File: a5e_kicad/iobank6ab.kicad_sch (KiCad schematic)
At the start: 1 part, among them U7 A5EB013B-B23B

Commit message: Power/config review against the Altera docs: bank 6A, MSEL, resets, fabric clock
Checked against Pin Connection Guidelines 813266, Power Management UG
813161, Configuration UG 813773 and the data sheet 813918; findings are
in AGILEX_POWER_CONFIG_CHECKLIST.md.

- VCCIO_HVIO_6A moves from the VCCPT 1V8 regulator to 3V3. PCG table 32
  requires a dedicated VCCIO_HVIO supply. CE19 no longer takes the 1.8 V
  sdm_clk25.
- Y4 (YXC OT3225100MJBA4SL, 100 MHz 3.3 V CMOS, C4353707) drives the
  dangling clk100 net to AE11 (bank 6G PLLREFCLK1), giving the fabric a
  PLL reference that doesn't depend on the HPS. The clock sheet pin
  clk2_N is renamed clk100.
- MSEL 001 (AS fast) -> 011 (AS normal): fast mode needs all supplies
  ramped within 10 ms, which the sequenced regulators don't guarantee.
  R45 now goes to 1V8, and R4 gets its own GND.
- R264 10k pull-up on HPS_COLD_nRESET (SDM_IO10), as the PCG requires.
- R9/R10 (INIT_DONE/CONF_DONE pull-ups) DNP; the internal pull-downs
  hold the pins low until configuration.
- Note on the fpga_power sheet and the PCB (Cmts.User): ferrite + cap
  isolation filters on the PLL/ADC rails are recommended but not
  fitted yet.
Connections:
- net sdm_clk25: no longer names the net of U7.CE19 (6A_IO_HVIO_6A_10_PLLREFCLK2_TXCLK10_RXCLK2_Data_Ctrl10)
- no-connect marks 3 -> 4
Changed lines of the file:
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@@
 	)
 	(bus_entry
-		(at 66.04 48.26)
-		(size 2.54 2.54)
-		(stroke
-			(width 0)
-			(type default)
-		)
-	)
-	(bus_entry
 		(at 66.04 88.9)
 		(size 2.54 2.54)
@@
 		)
 	)
-	(wire
-		(pts
-			(xy 68.58 50.8) (xy 96.52 50.8)
-		)
-		(stroke
-			(width 0)
-			(type default)
-		)
-	)
 	(bus
 		(pts
@@
 		)
 	)
-	(global_label "sdm_clk25"
-		(shape input)
-		(at 86.36 50.8 0)
-		(effects
-			(font
-				(size 1.27 1.27)
-			)
-			(justify left)
-		)
-		(property "Intersheetrefs" "${INTERSHEET_REFS}"
-			(at 86.36 50.8 0)
-			(hide yes)
-			(show_name no)
-			(do_not_autoplace no)
-			(effects
-				(font
-					(size 1.27 1.27)
-				)
-			)
-		)
-	)
 	(hierarchical_label "{iob6a}"
 		(shape bidirectional)
@@
 		)
 	)
+	(no_connect
+		(at 96.52 50.8)
+	)
 )

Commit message: LPDDR4 routing in progress: in-lane DQ swizzle (bytes 0, 2, 3), schematic and PCB
- iobank3: in-lane DQ swaps in byte 0 (BL1 dq3-dq6), byte 2 (BL7 dq17-dq23) and
  byte 3 (BL6 dq25/26/28/31); byte swizzle unchanged (1 0 X X X X 3 2).
- PCB: routing of bytes 0-3 in progress (DQ on F.Cu / In5, DQS/DM on In2); U7/U12
  pad nets match the schematic.
- Quartus test build (varA_sch1028) passes synthesis, fitter and timing with
  PIN_SWIZZLE DQS0=0 1 7 5 3 2 6 4, DQS1=8 15 9 14 13 12 10 11,
  DQS2=20 19 21 18 22 17 23 16, DQS3=27 26 29 28 31 30 24 25.
- Swizzle docs: lane map, Quartus strings, package delays per net updated; the
  swizzle is marked work in progress (more swaps while the other channel is routed).
- Other schematic sheet edits as in the working tree (bank 6A at 3.3 V, CE19 no
  longer takes sdm_clk25, etc.).
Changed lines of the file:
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@@
 	)
 	(no_connect
+		(at 96.52 50.8)
+	)
+	(no_connect
 		(at 96.52 116.84)
 	)
@@
 	(bus
 		(pts
-			(xy 66.04 48.26) (xy 66.04 50.8)
-		)
-		(stroke
-			(width 0)
-			(type default)
-		)
-	)
-	(bus
-		(pts
 			(xy 50.8 22.86) (xy 66.04 22.86)
 		)
@@
 	(bus
 		(pts
-			(xy 66.04 45.72) (xy 66.04 48.26)
+			(xy 66.04 45.72) (xy 66.04 50.8)
 		)
 		(stroke
@@
 		)
 	)
-	(no_connect
-		(at 96.52 50.8)
-	)
 )

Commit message: Schematic reorg step 1: remove dangling stubs and stale notes, correct notes, fill title blocks
Netlist: 0 renamed, 0 connectivity diffs; DRC parity 0. ERC 315 -> 242.
Plan refreshed for the eMMC, RTL8211FDI, TPS548A28 and the tuned LPDDR4 (IOBANK 3 sheet name kept).
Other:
- note added: "VCCIO_6B : 3V3"
- note removed: "VCCIO_6B : 2.5V or 3.3V"
- title: (none) -> Banks 6A / 6B HVIO
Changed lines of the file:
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@@
 	(paper "A4")
 	(title_block
-		(rev "0.1")
+		(title "Banks 6A / 6B HVIO")
+		(rev "${REVISION}")
+		(comment 1 "${BOARD}")
 	)
-	(text "VCCIO_6B : 2.5V or 3.3V"
+	(text "VCCIO_6B : 3V3"
 		(exclude_from_sim no)
 		(at 165.1 81.28 0)

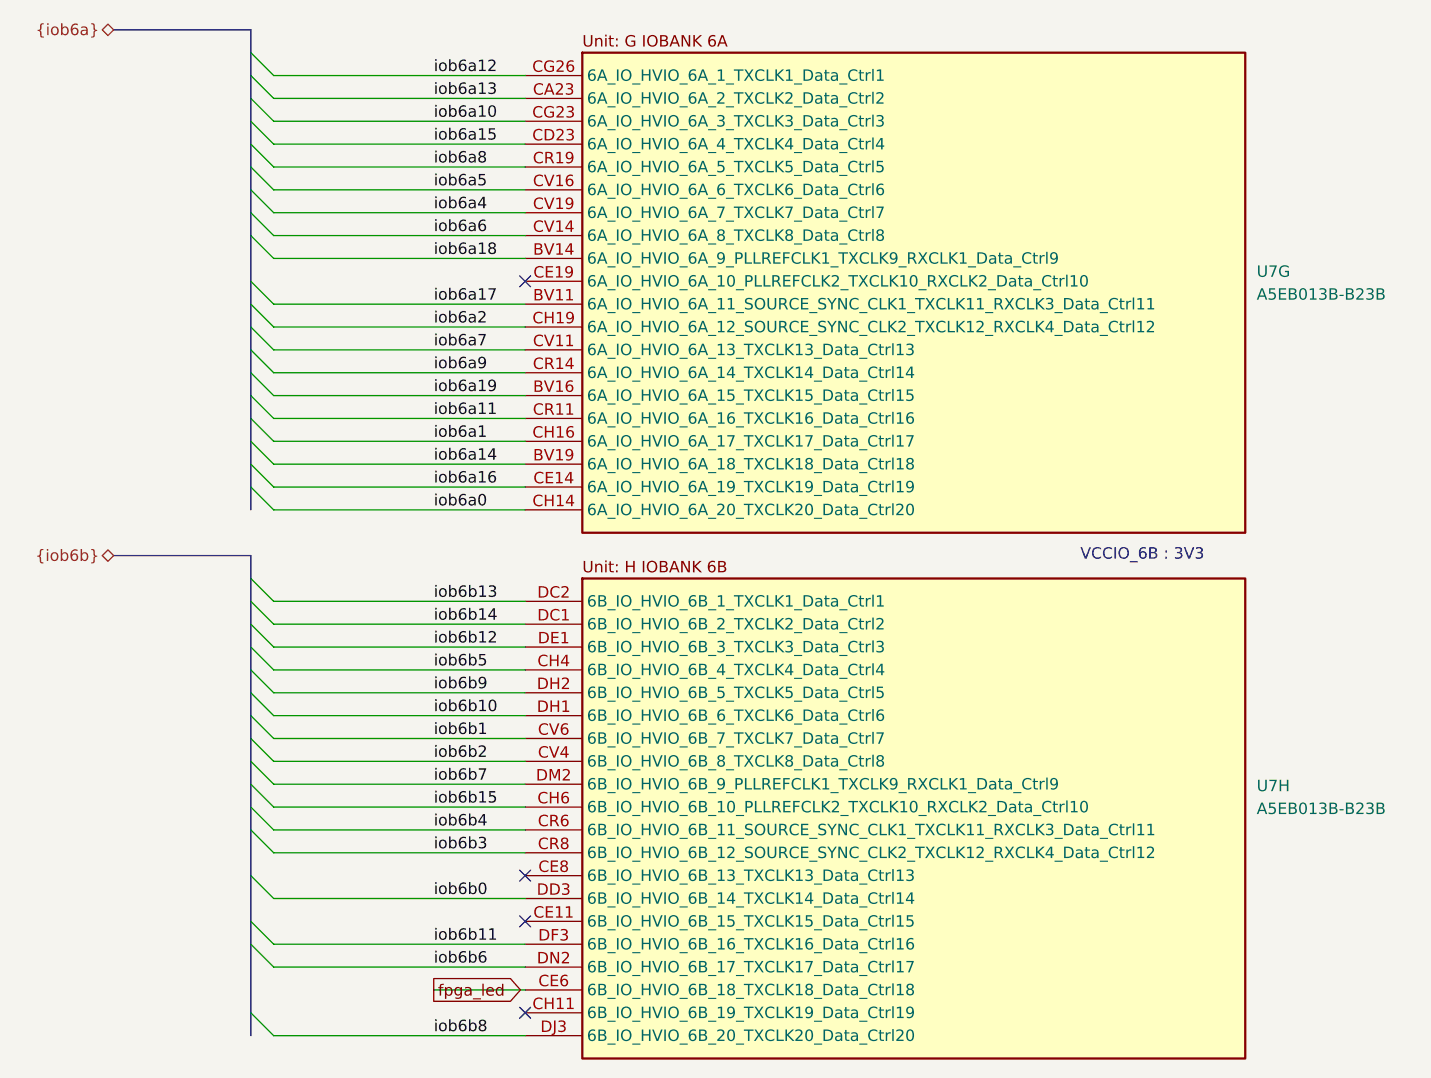
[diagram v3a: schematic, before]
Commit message: Schematic reorg step 7: no global labels, NC flags on unused U7 pins
- hps_uart0_tx/rx, eth_rst_n, phy_rst_n, fpga_led: global labels replaced by
  sheet pins; eth_led_g_n is a local label
- HyperBus labels/bus, the HPS {hps_i2c} bus and the pwr_scl/pwr_sda wiring
  removed (nothing behind them)
- 118 U7 pins that only had a net label: label, stub and bus entry removed,
  no-connect flag added
- Bank 3A notes restacked
- PCB: 124 nets renamed (118 to unconnected-(U7...))

Netdiff: 124 renamed, 0 connectivity diffs. ERC 148 -> 21. DRC parity 0.
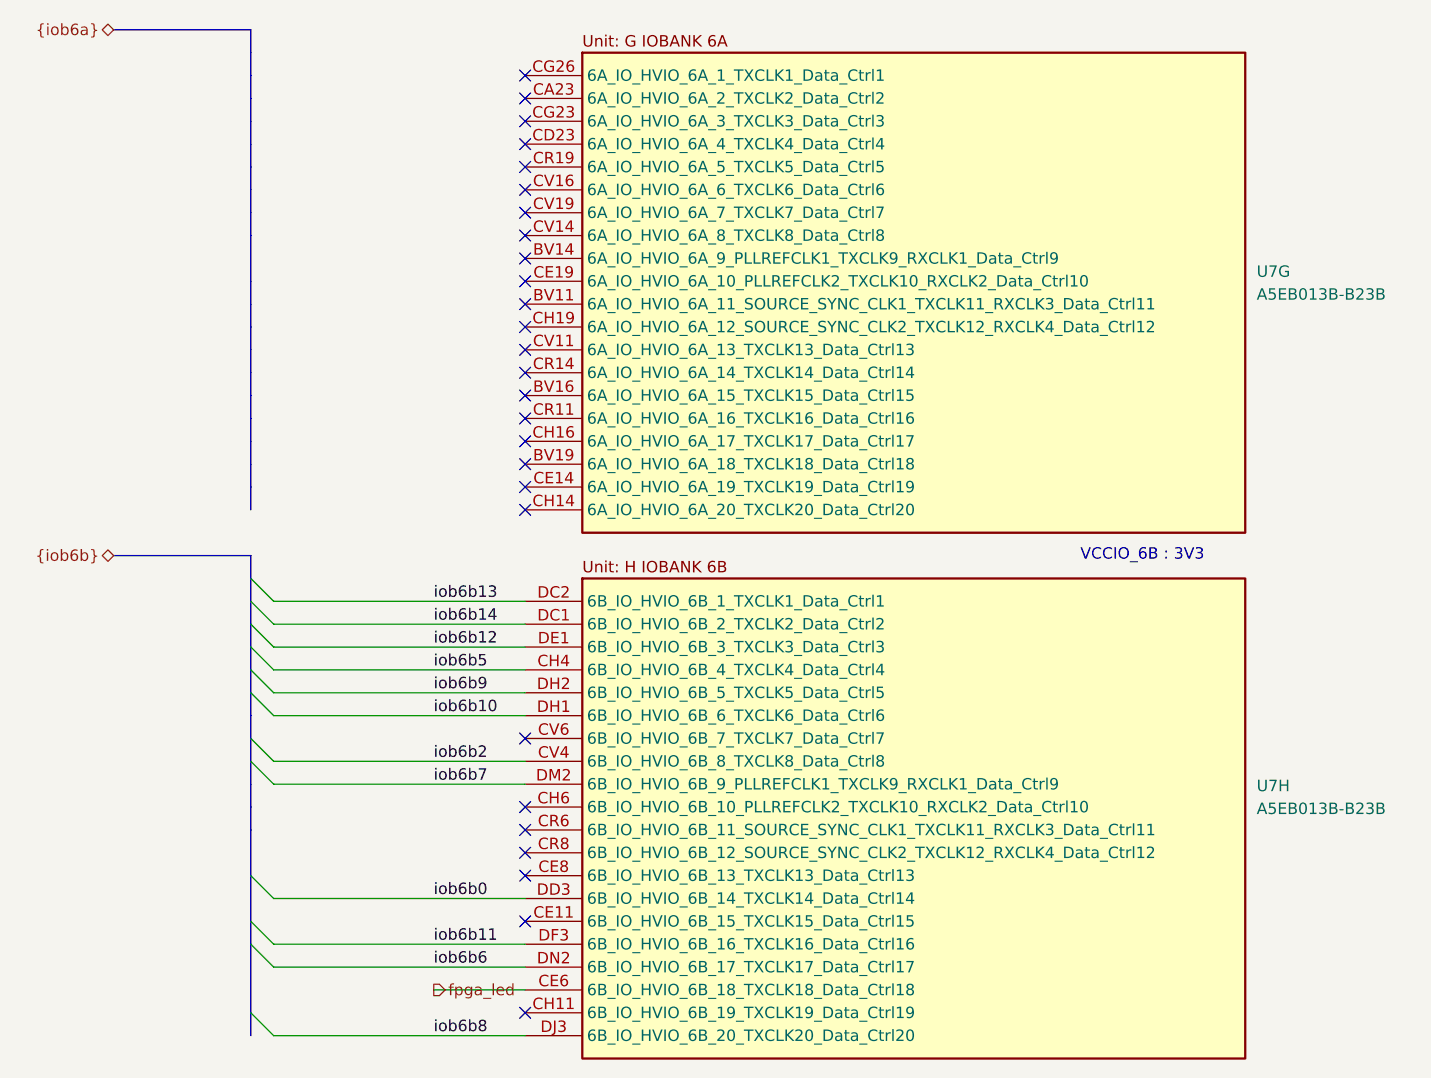
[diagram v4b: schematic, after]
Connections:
- net iob6a0: no longer names the net of U7.CH14 (6A_IO_HVIO_6A_20_TXCLK20_Data_Ctrl20)
- net iob6a1: no longer names the net of U7.CH16 (6A_IO_HVIO_6A_17_TXCLK17_Data_Ctrl17)
- net iob6a10: no longer names the net of U7.CG23 (6A_IO_HVIO_6A_3_TXCLK3_Data_Ctrl3)
- net iob6a11: no longer names the net of U7.CR11 (6A_IO_HVIO_6A_16_TXCLK16_Data_Ctrl16)
- net iob6a12: no longer names the net of U7.CG26 (6A_IO_HVIO_6A_1_TXCLK1_Data_Ctrl1)
- net iob6a13: no longer names the net of U7.CA23 (6A_IO_HVIO_6A_2_TXCLK2_Data_Ctrl2)
- net iob6a14: no longer names the net of U7.BV19 (6A_IO_HVIO_6A_18_TXCLK18_Data_Ctrl18)
- net iob6a15: no longer names the net of U7.CD23 (6A_IO_HVIO_6A_4_TXCLK4_Data_Ctrl4)
- net iob6a16: no longer names the net of U7.CE14 (6A_IO_HVIO_6A_19_TXCLK19_Data_Ctrl19)
- net iob6a17: no longer names the net of U7.BV11 (6A_IO_HVIO_6A_11_SOURCE_SYNC_CLK1_TXCLK11_RXCLK3_Data_Ctrl11)
- net iob6a18: no longer names the net of U7.BV14 (6A_IO_HVIO_6A_9_PLLREFCLK1_TXCLK9_RXCLK1_Data_Ctrl9)
- net iob6a19: no longer names the net of U7.BV16 (6A_IO_HVIO_6A_15_TXCLK15_Data_Ctrl15)
- net iob6a2: no longer names the net of U7.CH19 (6A_IO_HVIO_6A_12_SOURCE_SYNC_CLK2_TXCLK12_RXCLK4_Data_Ctrl12)
- net iob6a4: no longer names the net of U7.CV19 (6A_IO_HVIO_6A_7_TXCLK7_Data_Ctrl7)
- net iob6a5: no longer names the net of U7.CV16 (6A_IO_HVIO_6A_6_TXCLK6_Data_Ctrl6)
- net iob6a6: no longer names the net of U7.CV14 (6A_IO_HVIO_6A_8_TXCLK8_Data_Ctrl8)
- net iob6a7: no longer names the net of U7.CV11 (6A_IO_HVIO_6A_13_TXCLK13_Data_Ctrl13)
- net iob6a8: no longer names the net of U7.CR19 (6A_IO_HVIO_6A_5_TXCLK5_Data_Ctrl5)
- net iob6a9: no longer names the net of U7.CR14 (6A_IO_HVIO_6A_14_TXCLK14_Data_Ctrl14)
- net iob6b1: no longer names the net of U7.CV6 (6B_IO_HVIO_6B_7_TXCLK7_Data_Ctrl7)
- net iob6b15: no longer names the net of U7.CH6 (6B_IO_HVIO_6B_10_PLLREFCLK2_TXCLK10_RXCLK2_Data_Ctrl10)
- net iob6b3: no longer names the net of U7.CR8 (6B_IO_HVIO_6B_12_SOURCE_SYNC_CLK2_TXCLK12_RXCLK4_Data_Ctrl12)
- net iob6b4: no longer names the net of U7.CR6 (6B_IO_HVIO_6B_11_SOURCE_SYNC_CLK1_TXCLK11_RXCLK3_Data_Ctrl11)
- no-connect marks 4 -> 27
